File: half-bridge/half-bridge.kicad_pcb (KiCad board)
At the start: 4 copper layers, 59 x 36 mm, 81 parts, among them J1 Conn_01x11_Pin, J2 MountingHole_Pad, J3 Conn_01x11_Pin, J4 Conn_01x11_Pin, J5 Conn_01x11_Pin, J6 Conn_01x11_Pin, J7 MountingHole_Pad, J8 MountingHole_Pad, J9 MountingHole_Pad, Q1 EPC2306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

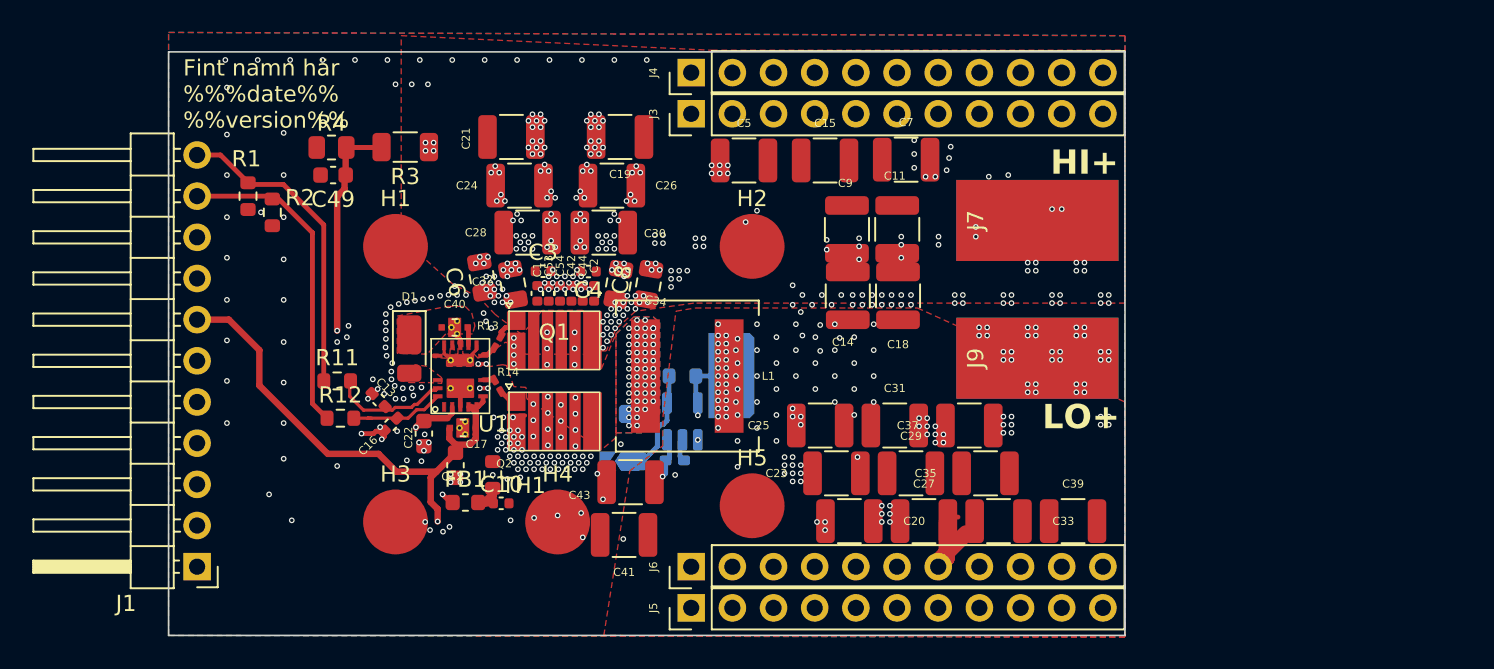
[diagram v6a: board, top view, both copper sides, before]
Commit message: Add diodes and make room for larger inductors
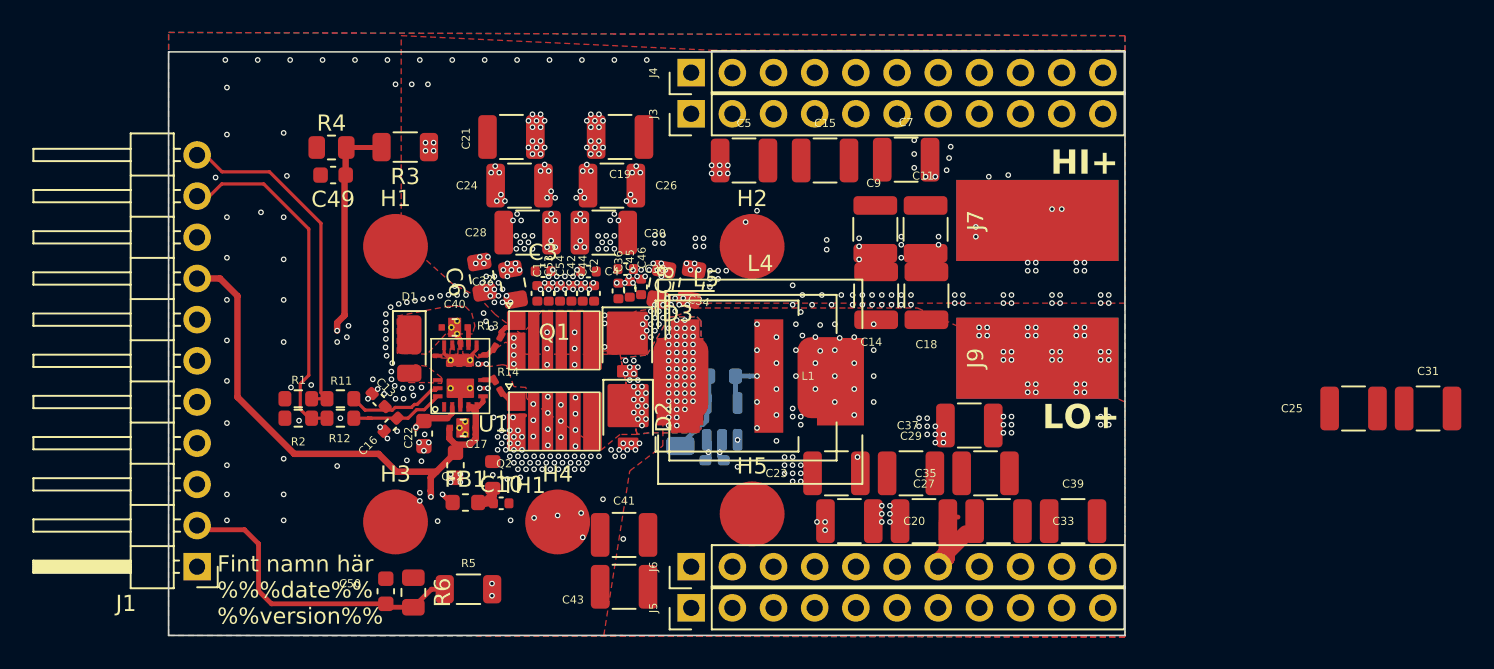
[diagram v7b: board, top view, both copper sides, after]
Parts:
- removed HS3: Heatsink_Pad, Library:Heatsink_SMD_Chamfered_5.2x5.2mm
- removed R15: 0R, Library:SolderJumper-2_P1.3mm_Open_TrianglePad1.0x1.2mm
- added C36: cap=1nF esr=72m srf=304MEG, Capacitor_SMD:C_0402_1005Metric, F.Cu at (137.8, 94.8)
- added C38: cap=1nF esr=72m srf=304MEG, Capacitor_SMD:C_0402_1005Metric, F.Cu at (138.2, 93.4)
- added C45: cap=1nF esr=72m srf=304MEG, Capacitor_SMD:C_0402_1005Metric, F.Cu at (138.4, 94.7)
- added C46: cap=1nF esr=72m srf=304MEG, Capacitor_SMD:C_0402_1005Metric, F.Cu at (139.2, 94.5)
- added C50: 1nF, Capacitor_SMD:C_0603_1608Metric, F.Cu at (123.4, 113.3)
- added D2: D_Schottky, Diode_SMD:D_SMP_DO-220AA, F.Cu at (138.3, 102.5)
- added D3: D_Schottky, Diode_SMD:D_SMP_DO-220AA, F.Cu at (138.3, 98.0)
- added L4: ~, Inductor_SMD:L_Wuerth_WE-PD-Typ-LS, F.Cu at (146.5, 100.3)
- added L5: ~, Inductor_SMD:L_Bourns_SRP1050WA, F.Cu at (146.1, 100.1)
- added R5: 100k, Resistor_SMD:R_1206_3216Metric, F.Cu at (128.5, 113.2)
- added R6: 10k, Resistor_SMD:R_0805_2012Metric, F.Cu at (125.1, 113.3)
- L1: value ind=3.75uH esr=9.77m epc=9.28pF -> ind=1.76uH esr=9.77m epc=9.28pF
- moved C25 32.9 mm to (183.1, 102.0)
- moved C31 32.9 mm to (187.7, 102.0)
- moved R1 12.9 mm to (118.0, 101.4), turned to 0 degrees
- moved R2 12.8 mm to (118.0, 102.6), turned to 0 degrees
- moved C43 6.46 mm to (138.1, 113.0)
- moved R26 3.08 mm to (141.6, 102.8)
- moved C34 2.65 mm to (140.4, 94.3)
- moved C8 2.65 mm to (142.2, 94.3)
- moved C47 2.45 mm to (144.2, 100.0)
- moved C48 2.45 mm to (143.7, 105.2)
- moved NT1 2.45 mm to (145.6, 100.0)
- moved U2 2.45 mm to (144.2, 102.8)
- moved L1 2.45 mm to (144.4, 100.0)
- moved C11 1.75 mm to (156.7, 91.0)
- moved C14 1.75 mm to (153.7, 95.0)
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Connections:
- net Current_sense+ renamed Current_sense
- C47 pad 2: Current_sense- -> Net-(U2--)
- J1 pad 2: Current_sense- -> FB_LOW
- NT1 pad 1: Current_sense- -> Net-(U2--)
- U2 pad 5: Current_sense- -> Net-(U2--)
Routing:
- net Current_sense-: track 37.8 -> 0.00 mm, vias 1 -> 0
- net FB_LOW: track 0.00 -> 19.5 mm
- net +5V: track 48.2 -> 52.1 mm
- net Current_sense: track 34.1 -> 36.7 mm, vias 2 -> 1
- net /HI: track 19.2 -> 21.3 mm
- net 0: track 12.4 -> 10.4 mm, vias 379 -> 394
- net Net-(U2--): track 0.00 -> 1.99 mm
- net /LI: track 19.9 -> 21.6 mm
- net /RC_current_sense: track 6.60 -> 5.11 mm
- net Net-(U1-EN/HI): track 7.29 -> 6.02 mm
- net POWER_LOW: track 0.00 -> 0.45 mm, vias 75 -> 52
- net Switch_node: track 3.92 -> 3.64 mm, vias 68 -> 88

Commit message: Add current sense resistors
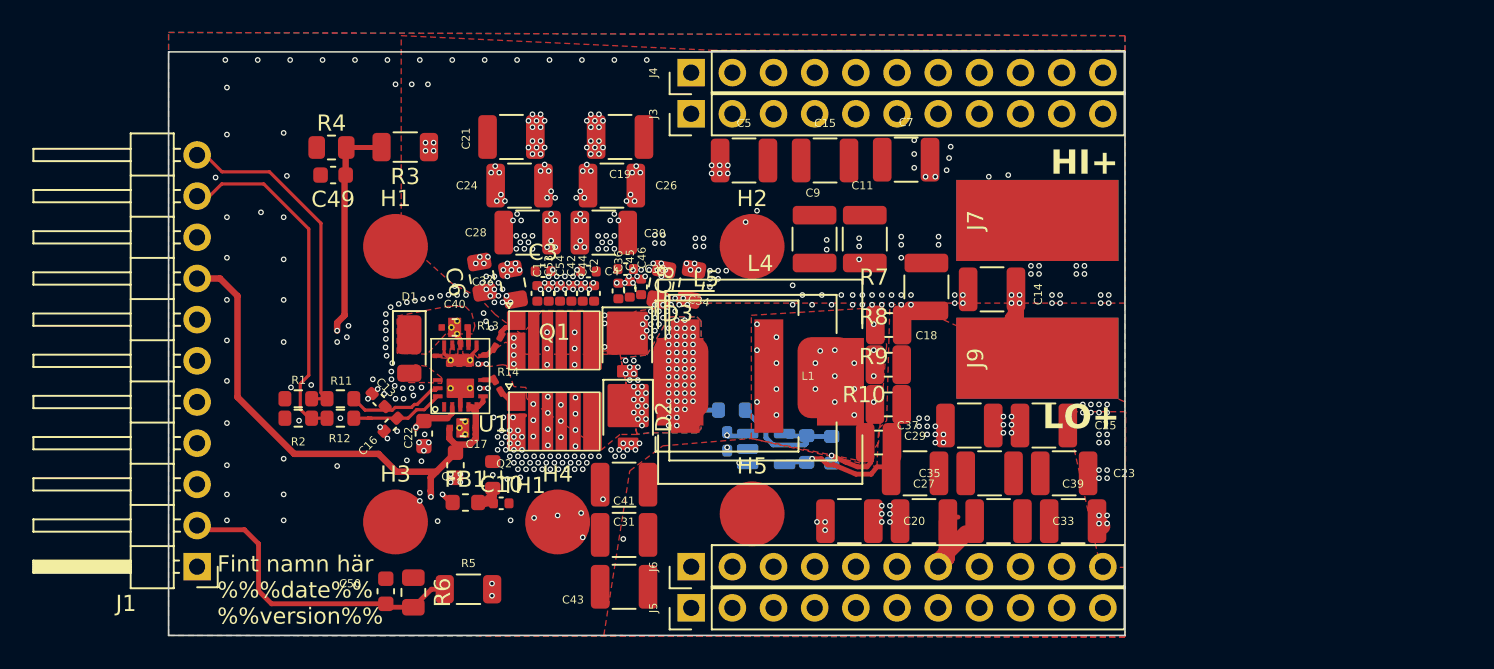
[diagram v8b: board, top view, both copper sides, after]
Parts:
- added NT2: NetTie_2, NetTie:NetTie-2_SMD_Pad0.5mm, B.Cu at (152.8, 105.6)
- added R10: 5mR, Library:R_0508_1220Metric, F.Cu at (153.8, 104.1)
- added R15: 10k, Resistor_SMD:R_0603_1608Metric, B.Cu at (150.9, 104.5)
- added R7: 5mR, Library:R_0508_1220Metric, F.Cu at (154.4, 96.8)
- added R8: 5mR, Library:R_0508_1220Metric, F.Cu at (154.4, 99.3)
- added R9: 5mR, Library:R_0508_1220Metric, F.Cu at (154.4, 101.8)
- NT1: moved to B.Cu
- R26: footprint Resistor_SMD:R_1206_3216Metric -> Resistor_SMD:R_0603_1608Metric
- moved C31 49.8 mm to (138.1, 106.7), turned to 180 degrees
- moved C25 19.1 mm to (164.0, 103.0), turned to 0 degrees
- moved C23 14.1 mm to (165.2, 106.0), turned to 0 degrees
- moved NT1 10.1 mm to (154.0, 105.6)
- moved C14 7.16 mm to (160.8, 94.7), turned to 180 degrees
- moved C47 6.89 mm to (149.4, 104.5), turned to -90 degrees
- moved C11 3.80 mm to (152.9, 91.5)
- moved C9 3.80 mm to (149.8, 91.5)
- moved R26 3.26 mm to (144.8, 102.1), turned to 0 degrees
- moved U2 3.20 mm to (146.9, 104.5), turned to 0 degrees
- moved C48 1.40 mm to (144.5, 104.0), turned to -90 degrees
- moved C18 0.55 mm to (156.8, 94.5)
- moved C29 0.25 mm to (156.1, 106.0)
- moved C35 0.25 mm to (160.7, 106.0)
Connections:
- L1 pad 2: POWER_LOW -> /I_Shunt
- L4 pad 2: POWER_LOW -> /I_Shunt
- L5 pad 2: POWER_LOW -> /I_Shunt
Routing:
- net Net-(U2--): track 1.99 -> 5.68 mm, vias 0 -> 1
- net /RC_current_sense: track 5.11 -> 8.20 mm
- net POWER_LOW: track 0.45 -> 3.00 mm, vias 52 -> 40
- net Switch_node: track 3.64 -> 5.73 mm
- net Net-(NT2-Pad1): track 0.00 -> 1.75 mm, vias 0 -> 1
- net /I_Shunt: track 0.00 -> 1.73 mm
- net +5V: track 52.1 -> 53.8 mm
- net Current_sense: track 36.7 -> 35.9 mm
- net 0: track 10.4 -> 9.67 mm, vias 394 -> 361
- net POWER_HIGH: vias 110 -> 106
- added copper zone on F.Cu, net /I_Shunt
- added copper zone on In2.Cu, net /I_Shunt
